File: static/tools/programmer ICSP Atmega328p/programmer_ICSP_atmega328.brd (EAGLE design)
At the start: 32.4 x 51.7 mm, 5 parts, among them IC1 MEGA8-P

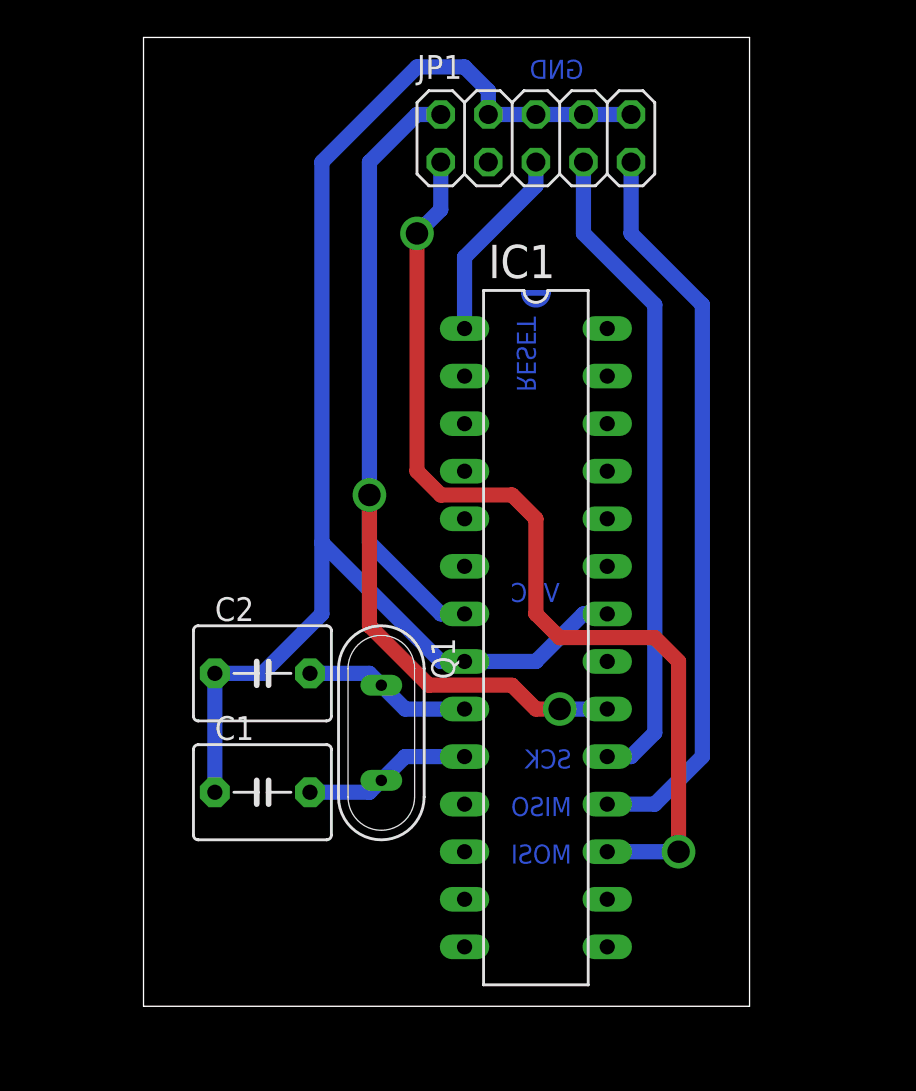
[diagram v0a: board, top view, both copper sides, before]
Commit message: [Programmer ICSP Atmega328p] smaller design
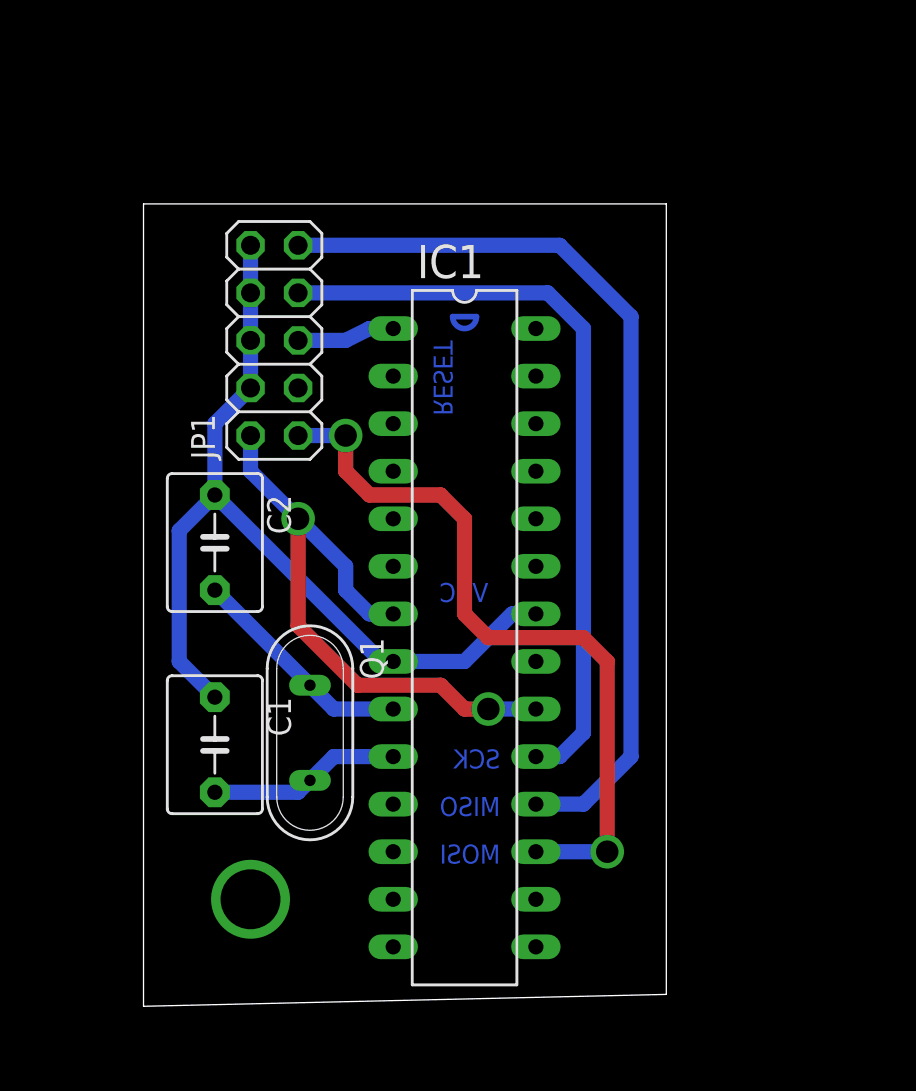
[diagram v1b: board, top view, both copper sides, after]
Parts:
- moved JP1 17.7 mm to (6.99, 35.6), turned to 90 degrees
- moved C2 7.43 mm to (3.81, 24.8), turned to 270 degrees
- moved IC1 3.81 mm to (17.1, 19.7)
- moved Q1 3.81 mm to (8.89, 14.6)
- moved C1 3.59 mm to (3.81, 14.0), turned to 270 degrees
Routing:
- net GND: track 76.8 -> 48.4 mm
- net VCC: track 53.4 -> 33.7 mm
- net N$1: track 52.2 -> 39.6 mm
- net N$4: track 39.5 -> 49.0 mm
- net N$3: track 35.1 -> 40.7 mm
- net N$2: track 10.5 -> 5.23 mm
- net N$5: track 9.04 -> 12.2 mm
- net N$6: track 9.04 -> 10.3 mm
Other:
- board size 32.4 x 51.7 mm -> 27.9 x 42.9 mm
- board text removed: "GND"

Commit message: [Programmer ICSP Atmega328p] optimise routing
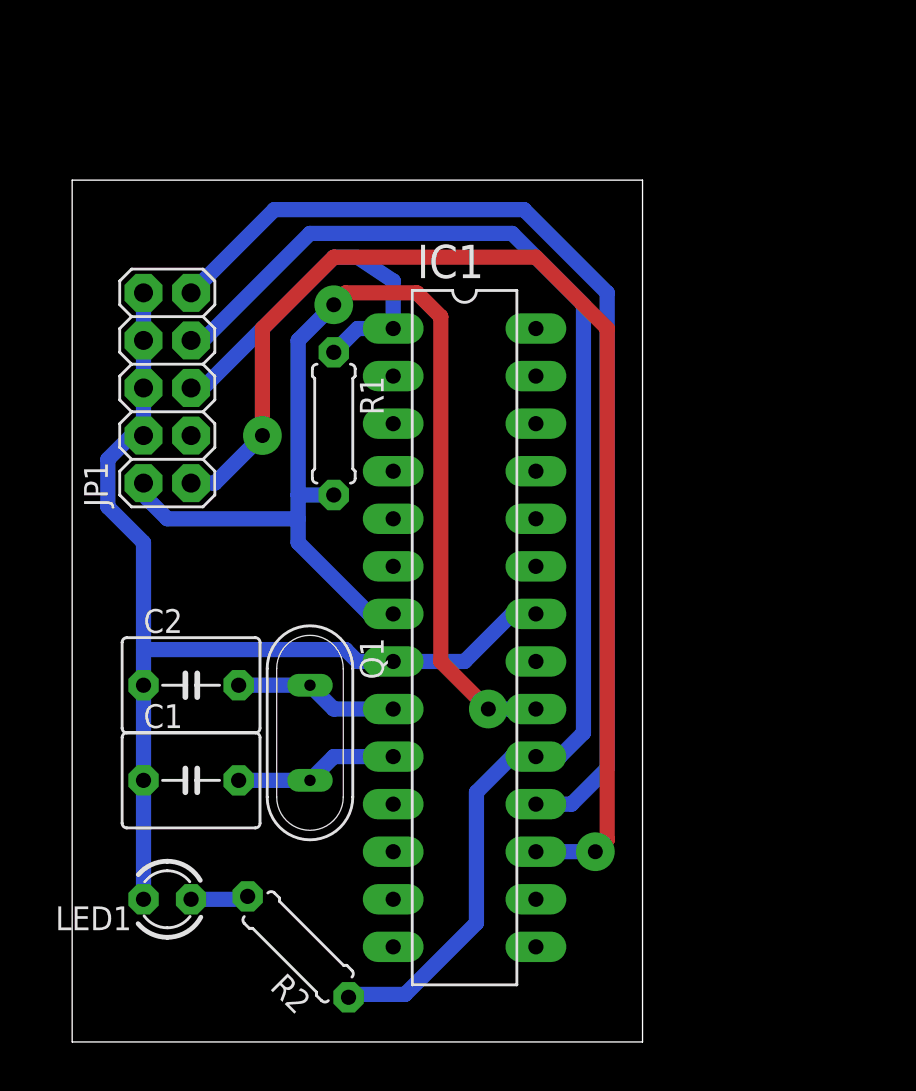
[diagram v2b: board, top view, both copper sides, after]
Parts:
- added LED1: (no value), led:LED3MM
- added R1, R2: (no value), rcl:0207/7
- moved C2 7.73 mm to (2.54, 17.1), turned to 0 degrees
- moved JP1 6.25 mm to (1.27, 33.0)
- moved C1 2.29 mm to (2.54, 12.1), turned to 0 degrees
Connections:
- new net JUJU: LED1.A, R2.2
- net GND: now also LED1.K
- net N$2: now also R1.1
- net N$3: now also R2.1
- net VCC: now also R1.2
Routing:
- net N$3: track 40.7 -> 70.2 mm
- net VCC: track 33.7 -> 62.5 mm
- net N$1: track 39.6 -> 63.5 mm
- net N$2: track 5.23 -> 20.3 mm
- net GND: track 48.4 -> 56.6 mm
- net N$4: track 49.0 -> 55.9 mm
- net N$5: track 12.2 -> 8.78 mm
- net JUJU: track 0.00 -> 3.08 mm
- net N$7: track 2.54 -> 0.00 mm
- net N$6: track 10.3 -> 8.78 mm
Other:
- board size 27.9 x 42.9 mm -> 30.5 x 46 mm
- board text removed: "MISO"
- board text removed: "MOSI"
- board text removed: "RESET"
- board text removed: "SCK"
- board text removed: "VCC"

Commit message: [Programmer ICSP Atmega328p] add capa values.
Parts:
- C1, C2: value (none) -> 20pF
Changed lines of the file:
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@@
 </element>
 <element name="Q1" library="special" package="QS" value="" x="8.89" y="14.605" rot="R270"/>
-<element name="C1" library="capacitor-wima" package="C5B5" value="" x="2.54" y="12.065"/>
-<element name="C2" library="capacitor-wima" package="C5B5" value="" x="2.54" y="17.145"/>
+<element name="C1" library="capacitor-wima" package="C5B5" value="20pF" x="2.54" y="12.065"/>
+<element name="C2" library="capacitor-wima" package="C5B5" value="20pF" x="2.54" y="17.145"/>
 <element name="R1" library="rcl" package="0207/7" value="" x="10.16" y="31.115" rot="R270"/>
 <element name="R2" library="rcl" package="0207/7" value="" x="8.255" y="3.175" rot="R135"/>

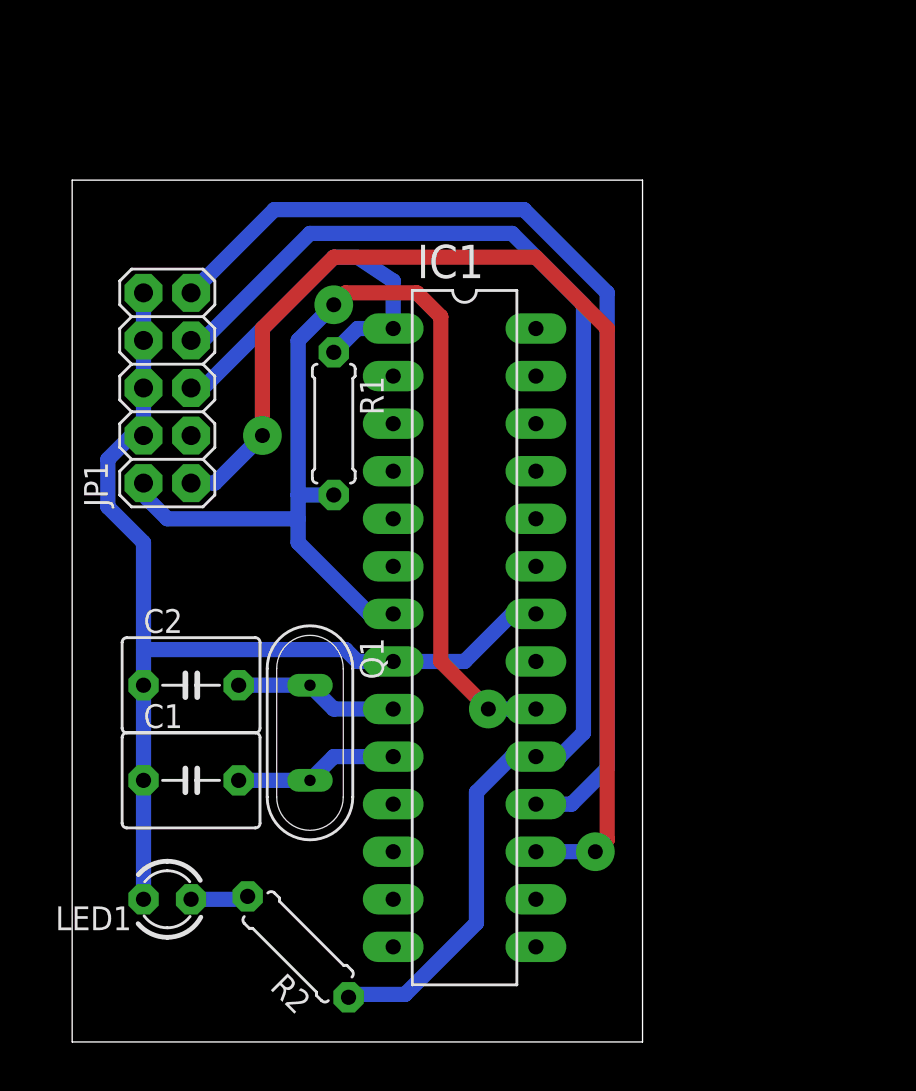
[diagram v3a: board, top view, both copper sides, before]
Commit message: [Porgrammer ICSP] Make another design for handle Attiny85
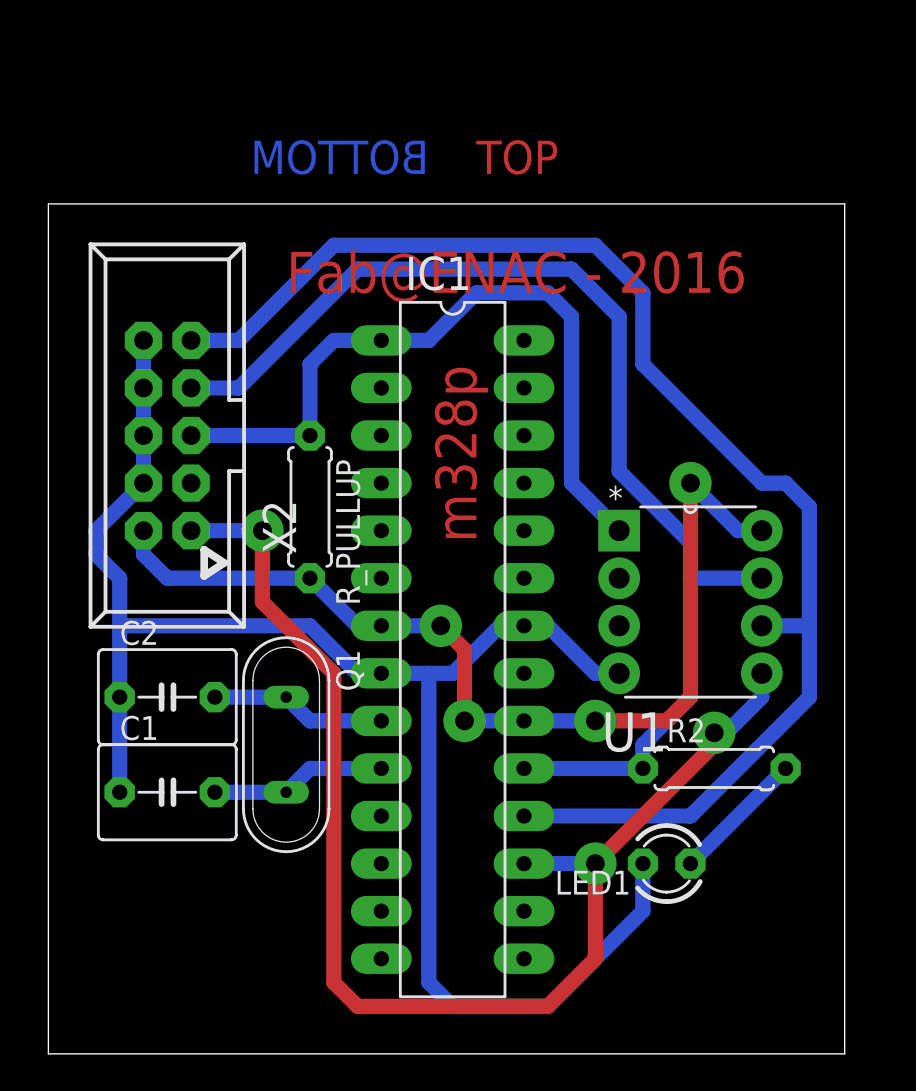
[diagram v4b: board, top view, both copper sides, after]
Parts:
- removed JP1: (no value), pinhead:2X05
- removed R1: (no value), rcl:0207/7
- added R_PULLUP: 5k, rcl:0207/7
- added U1: ATTINY85-20PU, Atmel_By_element14_Batch_1-00:DIP254P762X533-8
- added X2: 057-010-1, con-panduit:057-010-1
- R2: value (none) -> 220
- moved LED1 26.7 mm to (27.9, 7.62)
- moved R2 24.2 mm to (30.5, 12.7), turned to 0 degrees
- moved Q1 1.42 mm to (7.62, 14.0)
- moved C1 1.42 mm to (1.27, 11.4)
- moved C2 1.42 mm to (1.27, 16.5)
- moved IC1 0.90 mm to (16.5, 19.1)
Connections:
- removed net N$1: IC1.17, JP1.1
- removed net N$2: IC1.1, JP1.5, R1.1
- removed net N$3: IC1.19, JP1.7, R2.1
- removed net N$4: IC1.18, JP1.9
- new net MISO: IC1.18, U1.6, X2.9
- new net MOSI: IC1.17, U1.5, X2.1
- new net RESET: IC1.1, R_PULLUP.1, U1.1, X2.5
- new net SCK: IC1.19, R2.1, U1.7, X2.7
- net GND: now also U1.4, X2.10, X2.4, X2.6, X2.8; no longer JP1.10, JP1.4, JP1.6, JP1.8
- net VCC: now also R_PULLUP.2, U1.8, X2.2; no longer JP1.2, R1.2
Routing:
- net MISO: track 0.00 -> 73.7 mm
- net N$3: track 70.2 -> 0.00 mm
- net MOSI: track 0.00 -> 68.2 mm, vias 0 -> 3
- net N$1: track 63.5 -> 0.00 mm, vias 2 -> 0
- net SCK: track 0.00 -> 63.5 mm
- net N$4: track 55.9 -> 0.00 mm
- net RESET: track 0.00 -> 38.7 mm
- net GND: track 56.6 -> 88.6 mm
- net N$2: track 20.3 -> 0.00 mm
- net VCC: track 62.5 -> 53.2 mm, vias 2 -> 4
- net JUJU: track 3.08 -> 7.18 mm
- net N$5: track 8.78 -> 9.42 mm
- net N$6: track 8.78 -> 9.42 mm
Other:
- board size 30.5 x 46 mm -> 42.5 x 45.4 mm
- board text added: "BOTTOM"
- board text added: "Fab@ENAC - 2016"
- board text added: "TOP"
- board text added: "m328p"
